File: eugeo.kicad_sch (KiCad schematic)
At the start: 128 parts, among them J1 USB-C, J2 AVR_ISP, SW1 RESET, SW2 BOOT, U1 ATMEGA328P-PU, Y1 16MHz

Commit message: Add centre component cover
Lumberjack-style 2 mm acrylic cover over the diode stacks, MCU and USB-C,
held by four M2 10 mm standoffs. Adds mounting holes H9-H12 to the PCB
(rerouted, DRC clean, 49/49 functional checks), cover outline/DXF/gerbers,
a STEP/STL model, and a clearance check against parts and the case.

Co-Authored-By: Claude Opus 5.5 <noreply@anthropic.com>
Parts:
- added H10, H11, H12, H9: M2, eugeo:MountingHole_M2_NPTH, symbol eugeo:MountingHole
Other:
- note added: "Mounting holes (M2): H1-H8 case / plate, H9-H12 centre cover"
- note removed: "Mounting holes (M2)"
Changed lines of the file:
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@@
     )
   )
-  (text "Mounting holes (M2)" (at 332.74 104.14 0)
+  (text "Mounting holes (M2): H1-H8 case / plate, H9-H12 centre cover" (at 332.74 104.14 0)
     (effects (font (size 2 2)) (justify left bottom))
   )
@@
         )
       )
+    )
+  )
+  (symbol (lib_id "eugeo:MountingHole") (at 337.82 142.24 0) (unit 1)
+    (in_bom no) (on_board yes) (dnp no)
+    (property "Reference" "H9" (at 340.36 140.97 0)
+      (effects (font (size 1.27 1.27)))
+    )
+    (property "Value" "M2" (at 340.36 143.51 0)
+      (effects (font (size 1.27 1.27)))
+    )
+    (property "Footprint" "eugeo:MountingHole_M2_NPTH" (at 337.82 142.24 0)
+      (effects (font (size 1.27 1.27)) hide)
+    )
+    (property "Datasheet" "~" (at 337.82 142.24 0)
+      (effects (font (size 1.27 1.27)) hide)
+    )
+    (instances
+      (project "eugeo"
+        (path "/ac6326a6-577b-5382-9aa2-0aaf148fe34f"
+          (reference "H9") (unit 1)
+        )
+      )
+    )
+  )
+  (symbol (lib_id "eugeo:MountingHole") (at 353.06 142.24 0) (unit 1)
+    (in_bom no) (on_board yes) (dnp no)
+    (property "Reference" "H10" (at 355.6 140.97 0)
+      (effects (font (size 1.27 1.27)))
+    )
+    (property "Value" "M2" (at 355.6 143.51 0)
+      (effects (font (size 1.27 1.27)))
+    )
+    (property "Footprint" "eugeo:MountingHole_M2_NPTH" (at 353.06 142.24 0)
+      (effects (font (size 1.27 1.27)) hide)
+    )
+    (property "Datasheet" "~" (at 353.06 142.24 0)
+      (effects (font (size 1.27 1.27)) hide)
+    )
+    (instances
+      (project "eugeo"
+        (path "/ac6326a6-577b-5382-9aa2-0aaf148fe34f"
+          (reference "H10") (unit 1)
+        )
+      )
+    )
+  )
+  (symbol (lib_id "eugeo:MountingHole") (at 368.3 142.24 0) (unit 1)
+    (in_bom no) (on_board yes) (dnp no)
+    (property "Reference" "H11" (at 370.84 140.97 0)
+      (effects (font (size 1.27 1.27)))
+    )
+    (property "Value" "M2" (at 370.84 143.51 0)
+      (effects (font (size 1.27 1.27)))
+    )
+    (property "Footprint" "eugeo:MountingHole_M2_NPTH" (at 368.3 142.24 0)
+      (effects (font (size 1.27 1.27)) hide)
+    )
+    (property "Datasheet" "~" (at 368.3 142.24 0)
+      (effects (font (size 1.27 1.27)) hide)
+    )
+    (instances
+      (project "eugeo"
+        (path "/ac6326a6-577b-5382-9aa2-0aaf148fe34f"
+          (reference "H11") (unit 1)
+        )
+      )
+    )
+  )
+  (symbol (lib_id "eugeo:MountingHole") (at 383.54 142.24 0) (unit 1)
+    (in_bom no) (on_board yes) (dnp no)
+    (property "Reference" "H12" (at 386.08 140.97 0)
+      (effects (font (size 1.27 1.27)))
+    )
+    (property "Value" "M2" (at 386.08 143.51 0)
+      (effects (font (size 1.27 1.27)))
+    )
+    (property "Footprint" "eugeo:MountingHole_M2_NPTH" (at 383.54 142.24 0)
+      (effects (font (size 1.27 1.27)) hide)
+    )
+    (property "Datasheet" "~" (at 383.54 142.24 0)
+      (effects (font (size 1.27 1.27)) hide)
+    )
+    (instances
+      (project "eugeo"
+        (path "/ac6326a6-577b-5382-9aa2-0aaf148fe34f"
+          (reference "H12") (unit 1)
+        )
+      )

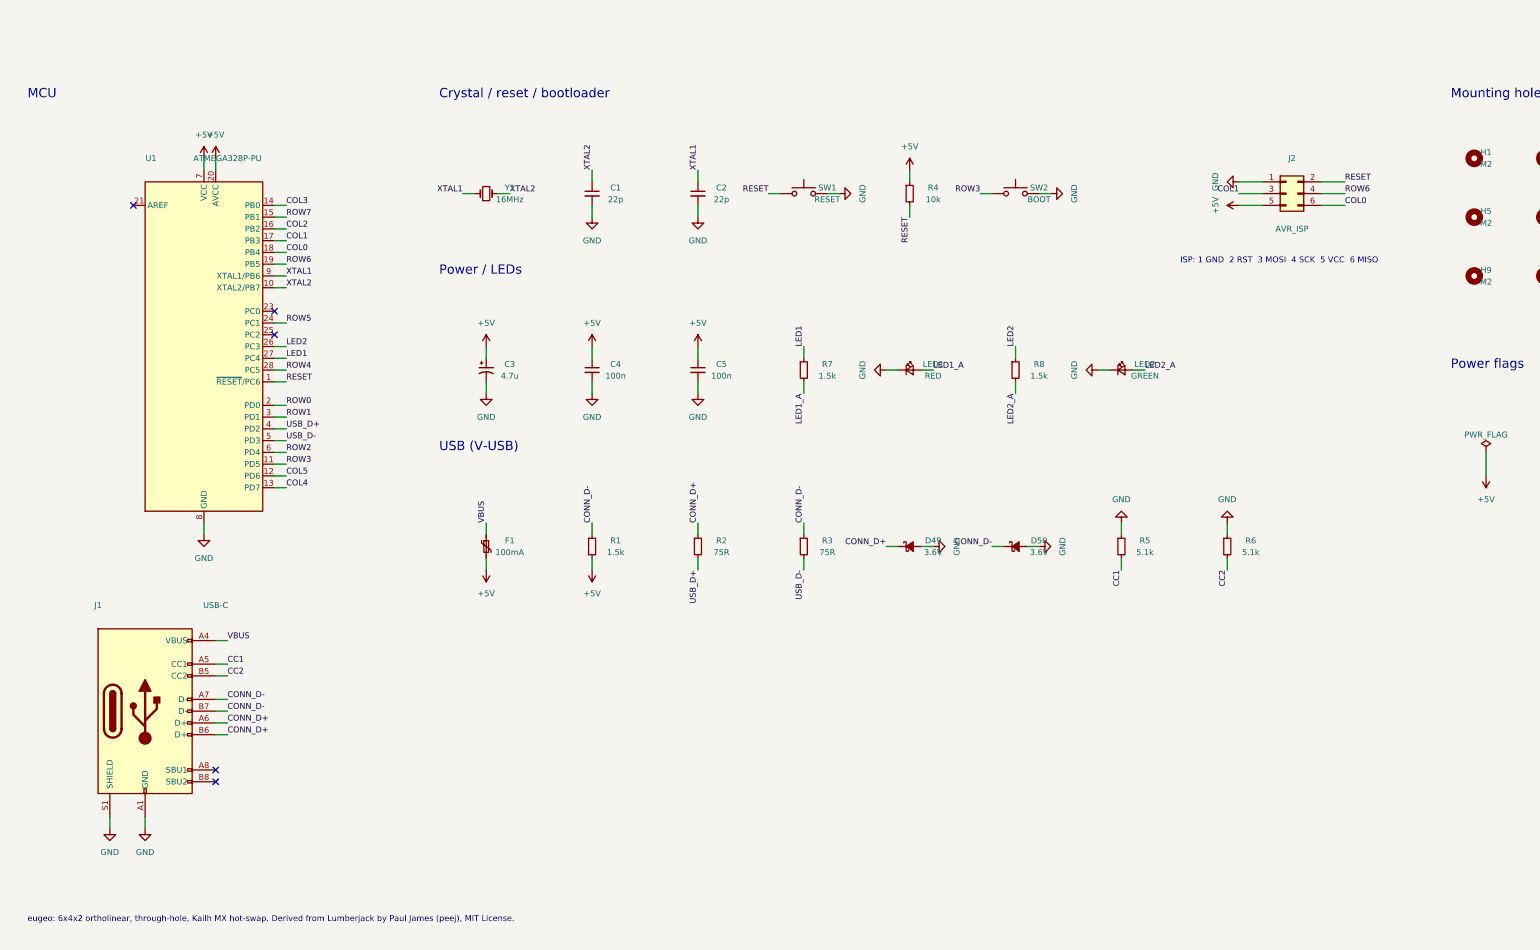
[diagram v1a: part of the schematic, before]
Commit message: Switch to RP2040, zigzag diodes and a frozen-stump back
- MCU: ATmega328P + V-USB -> RP2040 + W25Q16 QSPI flash, 12 MHz crystal,
  MCP1700 3.3 V LDO, USBLC6 ESD and 27R series resistors. SMD parts are
  assembled by JLCPCB (BOM/CPL now include them); everything else stays
  through-hole and on show.
- RP2040 block is hand-routed: +3V3 ring inside the pin ring, +1V1 via the
  back, QSPI / crystal / decoupling / row and column escapes. ISP and SWD
  headers dropped (UF2 flashing over USB with BOOT + RESET).
- Diode stacks zigzag like Lumberjack.
- Back side artwork: frozen tree stump with frost ferns and snowflakes,
  some as bare-copper mask openings (scripts/stump_art.py).
- QMK: RP2040 / rp2040 bootloader, new GP pin map, prebuilt UF2 files.
- verify_design.py rewritten for RP2040 (59 checks), preorder checks 23/23.
- Case support pillar moved clear of U4; cover, plates and laser-cut SVGs
  regenerated for the new cover holes.

Co-Authored-By: Claude Opus 5.5 <noreply@anthropic.com>
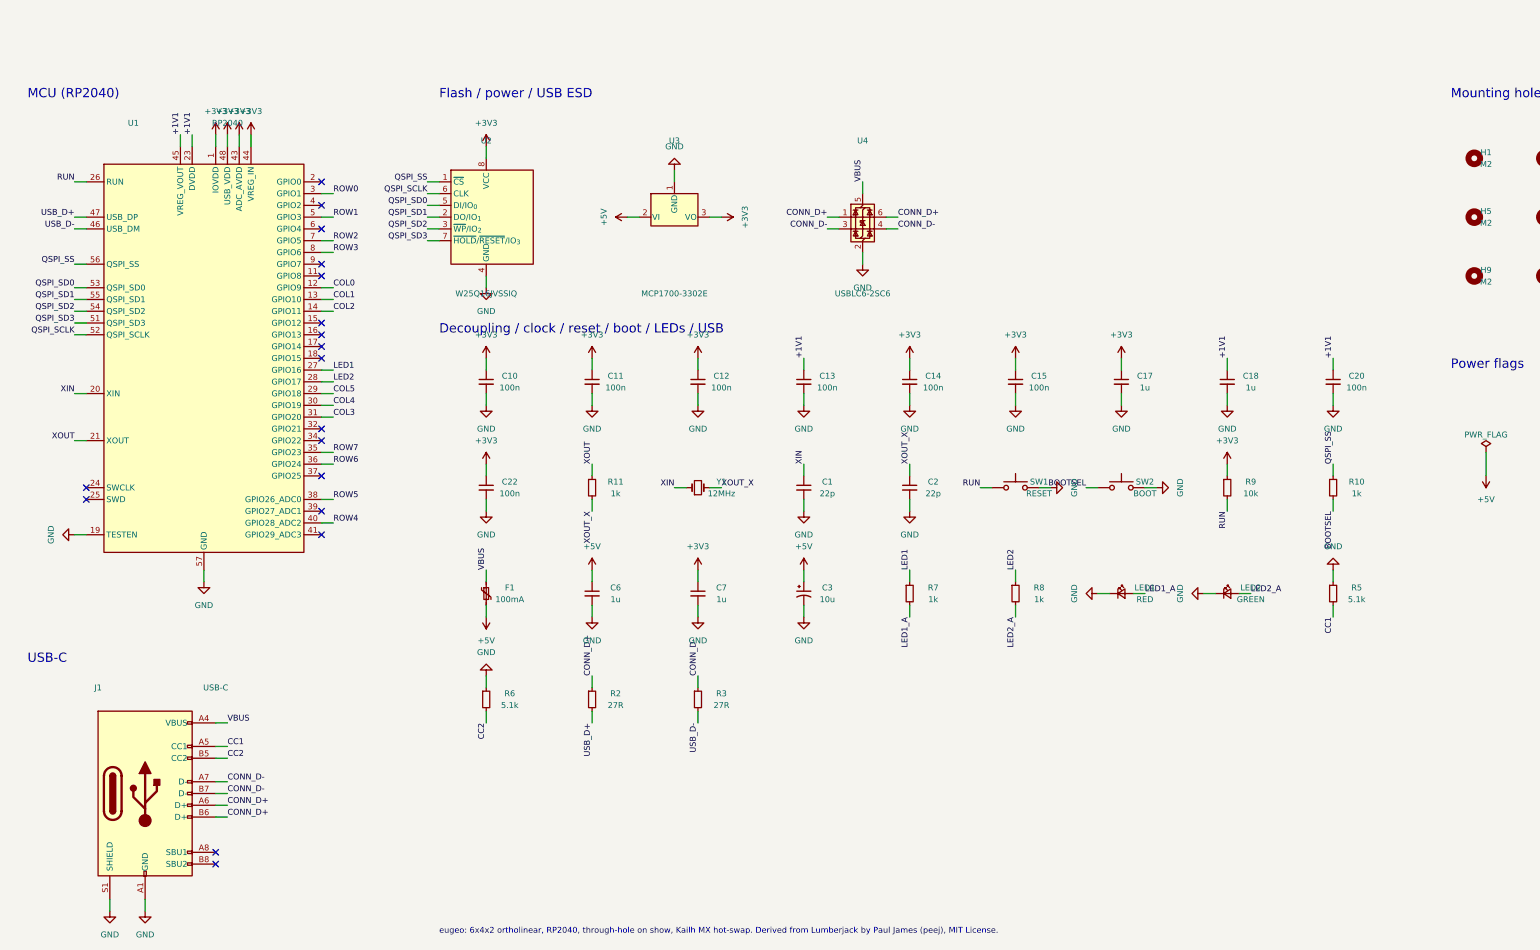
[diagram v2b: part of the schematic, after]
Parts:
- removed C4, C5: 100n, Capacitor_THT:C_Disc_D4.3mm_W1.9mm_P5.00mm, symbol eugeo:C_Small
- removed D49, D50: 3.6V, Diode_THT:D_DO-35_SOD27_P7.62mm_Horizontal, symbol eugeo:D_Zener_Small_ALT
- removed J2: AVR_ISP, Connector_PinHeader_2.54mm:PinHeader_2x03_P2.54mm_Vertical, symbol eugeo:Conn_02x03_Odd_Even
- removed R1: 1.5k, Resistor_THT:R_Axial_DIN0204_L3.6mm_D1.6mm_P7.62mm_Horizontal, symbol eugeo:R_Small
- removed R4: 10k, Resistor_THT:R_Axial_DIN0204_L3.6mm_D1.6mm_P7.62mm_Horizontal, symbol eugeo:R_Small
- added C10, C11, C12, C13, C14, C15, C20, C22: 100n, Capacitor_SMD:C_0402_1005Metric, symbol eugeo:C_Small
- added C17, C18: 1u, Capacitor_SMD:C_0402_1005Metric, symbol eugeo:C_Small
- added C6, C7: 1u, Capacitor_THT:C_Disc_D3.0mm_W2.0mm_P2.50mm, symbol eugeo:C_Small
- added R10: 1k, Resistor_THT:R_Axial_DIN0204_L3.6mm_D1.6mm_P7.62mm_Horizontal, symbol eugeo:R_Small
- added R11: 1k, Resistor_SMD:R_0402_1005Metric, symbol eugeo:R_Small
- added R9: 10k, Resistor_THT:R_Axial_DIN0204_L3.6mm_D1.6mm_P7.62mm_Horizontal, symbol eugeo:R_Small
- added U2: W25Q16JVSSIQ, Package_SO:SOIC-8_5.3x5.3mm_P1.27mm, symbol eugeo:W25Q16JVSS
- added U3: MCP1700-3302E, Package_TO_SOT_THT:TO-92_Inline_Wide, symbol eugeo:MCP1700-3302E_TO
- added U4: USBLC6-2SC6, Package_TO_SOT_SMD:SOT-23-6, symbol eugeo:USBLC6-2SC6
- C3: value 4.7u -> 10u
- R2, R3: value 75R -> 27R
- R7, R8: value 1.5k -> 1k
- U1: value ATMEGA328P-PU -> RP2040; footprint Package_DIP:DIP-28_W7.62mm -> Package_DFN_QFN:QFN-56-1EP_7x7mm_P0.4mm_EP3.2x3.2mm; symbol eugeo:ATmega328P-PU -> eugeo:RP2040
- Y1: value 16MHz -> 12MHz
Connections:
- net +5V: now also C6.1, U3.2 (VI); no longer U1.20 (AVCC), U1.7 (VCC)
- net COL0: now also U1.12 (GPIO9); no longer U1.18 (PB4)
- net COL1: now also U1.13 (GPIO10); no longer U1.17 (PB3)
- net COL2: now also U1.14 (GPIO11); no longer U1.16 (PB2)
- net COL3: now also U1.31 (GPIO20); no longer U1.14 (PB0)
- net COL4: now also U1.30 (GPIO19); no longer U1.13 (PD7)
- net COL5: now also U1.29 (GPIO18); no longer U1.12 (PD6)
- net CONN_D+: now also U4.1 (I/O1), U4.6 (I/O1)
- net CONN_D-: now also U4.3 (I/O2), U4.4 (I/O2)
- net GND: now also U1.19 (TESTEN), U1.57 (GND), C10.2, C11.2, C12.2, C13.2, C14.2, C15.2, C17.2, C18.2, C20.2, C22.2, C6.2, C7.2, U2.4 (GND), U3.1 (GND), U4.2 (GND); no longer U1.22 (GND), U1.8 (GND)
- net LED2: now also U1.28 (GPIO17); no longer U1.26 (PC3)
- net ROW0: now also U1.3 (GPIO1); no longer U1.2 (PD0)
- net ROW1: now also U1.5 (GPIO3); no longer U1.3 (PD1)
- net ROW2: now also U1.7 (GPIO5); no longer U1.6 (PD4)
- net ROW3: now also U1.8 (GPIO6); no longer SW2.1, U1.11 (PD5)
- net ROW4: now also U1.40 (GPIO28_ADC2); no longer U1.28 (PC5)
- net ROW5: now also U1.38 (GPIO26_ADC0); no longer U1.24 (PC1)
- net ROW6: now also U1.36 (GPIO24); no longer U1.19 (PB5)
- net ROW7: now also U1.35 (GPIO23); no longer U1.15 (PB1)
- net USB_D+: now also U1.47 (USB_DP); no longer U1.4 (PD2)
- net USB_D-: now also U1.46 (USB_DM); no longer U1.5 (PD3)
- net VBUS: now also U4.5 (VBUS)
- net XOUT: now reaches U1.21 (XOUT)
- net XOUT: now also R11.1
- net +1V1: now reaches U1.23 (DVDD)
- net +1V1: now also U1.45 (VREG_VOUT), U1.50 (DVDD), C13.1, C18.1, C20.1
- net RESET renamed +3V3
- net +3V3: now also U1.10 (IOVDD), U1.22 (IOVDD), U1.33 (IOVDD), U1.42 (IOVDD), U1.43 (ADC_AVDD), U1.44 (VREG_IN), U1.48 (USB_VDD), U1.49 (IOVDD), C10.1, C11.1, C12.1, C14.1, C15.1, C17.1, C22.1, C7.1, R9.1, U2.8 (VCC), U3.3 (VO); no longer SW1.1
- removed net XTAL1: C2.1, U1.9 (XTAL1/PB6), Y1.1
- removed net XTAL2: C1.1, U1.10 (XTAL2/PB7), Y1.2
- new net BOOTSEL: R10.2, SW2.1
- new net QSPI_SCLK: U1.52 (QSPI_SCLK), U2.6 (CLK)
- new net QSPI_SD0: U1.53 (QSPI_SD0), U2.5 (DI/IO_{0})
- new net QSPI_SD1: U1.55 (QSPI_SD1), U2.2 (DO/IO_{1})
- new net QSPI_SD2: U1.54 (QSPI_SD2), U2.3 (~{WP}/IO_{2})
- new net QSPI_SD3: U1.51 (QSPI_SD3), U2.7 (~{HOLD}/~{RESET}/IO_{3})
- new net QSPI_SS: R10.1, U1.56 (QSPI_SS), U2.1 (~{CS})
- new net RUN: R9.2, SW1.1, U1.26 (RUN)
- new net XIN: C1.1, U1.20 (XIN), Y1.1
- new net XOUT_X: C2.1, R11.2, Y1.2
- no-connect marks 5 -> 18
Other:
- note added: "Decoupling / clock / reset / boot / LEDs / USB"
- note added: "Flash / power / USB ESD"
- note added: "MCU (RP2040)"
- note added: "USB-C"
- note added: "eugeo: 6x4x2 ortholinear, RP2040, through-hole on show, Kailh MX hot-swap. Derived from Lumberjack by Paul James (peej), MIT License."
- note removed: "Crystal / reset / bootloader"
- note removed: "ISP: 1 GND 2 RST 3 MOSI 4 SCK 5 VCC 6 MISO"
- note removed: "MCU"
- note removed: "Power / LEDs"
- note removed: "USB (V-USB)"
- note removed: "eugeo: 6x4x2 ortholinear, through-hole, Kailh MX hot-swap. Derived from Lumberjack by Paul James (peej), MIT License."
- moved on the sheet: C1, C2, C3, F1, J1, LED1, LED2, R2, R3, R5, R6, R7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

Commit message: Move the status LEDs to the top, side by side
LED1 / LED2 now sit next to each other above the QSPI flash. They are
driven from the two topmost left GPIOs (GP2 / GP1) through 0402 resistors
on the back, which frees the crowded bottom-right corner. Left rows move
to GP3-GP6; QMK pins and the UF2 builds follow.

Co-Authored-By: Claude Opus 5.5 <noreply@anthropic.com>
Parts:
- R7, R8: footprint Resistor_THT:R_Axial_DIN0204_L3.6mm_D1.6mm_P7.62mm_Horizontal -> Resistor_SMD:R_0402_1005Metric
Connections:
- net LED1: now also U1.4 (GPIO2); no longer U1.27 (GPIO16)
- net LED2: now also U1.3 (GPIO1); no longer U1.28 (GPIO17)
- net ROW0: now also U1.5 (GPIO3); no longer U1.3 (GPIO1)
- net ROW1: now also U1.6 (GPIO4); no longer U1.5 (GPIO3)
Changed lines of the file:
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@@
     (stroke (width 0) (type default))
   )
-  (label "ROW0" (at 91.44 124.46 0) (fields_autoplaced)
-    (effects (font (size 1.27 1.27)) (justify left bottom))
-  )
-  (no_connect (at 88.9 127))
+  (label "LED2" (at 91.44 124.46 0) (fields_autoplaced)
+    (effects (font (size 1.27 1.27)) (justify left bottom))
+  )
+  (wire (pts (xy 88.9 127) (xy 91.44 127))
+    (stroke (width 0) (type default))
+  )
+  (label "LED1" (at 91.44 127 0) (fields_autoplaced)
+    (effects (font (size 1.27 1.27)) (justify left bottom))
+  )
   (wire (pts (xy 88.9 129.54) (xy 91.44 129.54))
     (stroke (width 0) (type default))
   )
-  (label "ROW1" (at 91.44 129.54 0) (fields_autoplaced)
-    (effects (font (size 1.27 1.27)) (justify left bottom))
-  )
-  (no_connect (at 88.9 132.08))
+  (label "ROW0" (at 91.44 129.54 0) (fields_autoplaced)
+    (effects (font (size 1.27 1.27)) (justify left bottom))
+  )
+  (wire (pts (xy 88.9 132.08) (xy 91.44 132.08))
+    (stroke (width 0) (type default))
+  )
+  (label "ROW1" (at 91.44 132.08 0) (fields_autoplaced)
+    (effects (font (size 1.27 1.27)) (justify left bottom))
+  )
   (wire (pts (xy 88.9 134.62) (xy 91.44 134.62))
     (stroke (width 0) (type default))
@@
   (no_connect (at 88.9 157.48))
   (no_connect (at 88.9 160.02))
-  (wire (pts (xy 88.9 162.56) (xy 91.44 162.56))
-    (stroke (width 0) (type default))
-  )
-  (label "LED1" (at 91.44 162.56 0) (fields_autoplaced)
-    (effects (font (size 1.27 1.27)) (justify left bottom))
-  )
-  (wire (pts (xy 88.9 165.1) (xy 91.44 165.1))
-    (stroke (width 0) (type default))
-  )
-  (label "LED2" (at 91.44 165.1 0) (fields_autoplaced)
-    (effects (font (size 1.27 1.27)) (justify left bottom))
-  )
+  (no_connect (at 88.9 162.56))
+  (no_connect (at 88.9 165.1))
   (wire (pts (xy 88.9 167.64) (xy 91.44 167.64))
     (stroke (width 0) (type default))
@@
       (effects (font (size 1.27 1.27)))
     )
-    (property "Footprint" "Resistor_THT:R_Axial_DIN0204_L3.6mm_D1.6mm_P7.62mm_Horizontal" (at 215.9 210.82 0)
+    (property "Footprint" "Resistor_SMD:R_0402_1005Metric" (at 215.9 210.82 0)
       (effects (font (size 1.27 1.27)) hide)
     )
@@
       (effects (font (size 1.27 1.27)))
     )
-    (property "Footprint" "Resistor_THT:R_Axial_DIN0204_L3.6mm_D1.6mm_P7.62mm_Horizontal" (at 238.76 210.82 0)
-      (effects (font (size 1.27 1.27)) hide)
-    )
+    (property "Footprint" "Resistor_SMD:R_0402_1005Metric" (at 238.76 210.82 0)
+      (effects (font (size 1.27 1.27)) hide)
+    )

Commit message: Balance the centre layout: LEDs left and right, parts mirrored
- One LED on each side at the top (under R5/R6 and R2/R3), driven from the
  topmost left / right GPIO (GP1 / GP28); right rows move to GP23-GP26.
- USB D+/D- go round the right LED to R2/R3.
- Lower parts mirrored about the centre line: U3 | crystal | F1, the four
  disc capacitors in one row, R9 / R10 between RESET and BOOT, C3 centred.

Co-Authored-By: Claude Opus 5.5 <noreply@anthropic.com>
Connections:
- net LED1: now also U1.3 (GPIO1); no longer U1.4 (GPIO2)
- net LED2: now also U1.40 (GPIO28_ADC2); no longer U1.3 (GPIO1)
- net ROW4: now also U1.38 (GPIO26_ADC0); no longer U1.40 (GPIO28_ADC2)
- net ROW5: now also U1.37 (GPIO25); no longer U1.38 (GPIO26_ADC0)
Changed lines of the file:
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@@
     (stroke (width 0) (type default))
   )
-  (label "LED2" (at 91.44 124.46 0) (fields_autoplaced)
+  (label "LED1" (at 91.44 124.46 0) (fields_autoplaced)
     (effects (font (size 1.27 1.27)) (justify left bottom))
   )
-  (wire (pts (xy 88.9 127) (xy 91.44 127))
-    (stroke (width 0) (type default))
-  )
-  (label "LED1" (at 91.44 127 0) (fields_autoplaced)
-    (effects (font (size 1.27 1.27)) (justify left bottom))
-  )
+  (no_connect (at 88.9 127))
   (wire (pts (xy 88.9 129.54) (xy 91.44 129.54))
     (stroke (width 0) (type default))
@@
     (effects (font (size 1.27 1.27)) (justify left bottom))
   )
-  (no_connect (at 88.9 185.42))
+  (wire (pts (xy 88.9 185.42) (xy 91.44 185.42))
+    (stroke (width 0) (type default))
+  )
+  (label "ROW5" (at 91.44 185.42 0) (fields_autoplaced)
+    (effects (font (size 1.27 1.27)) (justify left bottom))
+  )
   (wire (pts (xy 88.9 190.5) (xy 91.44 190.5))
     (stroke (width 0) (type default))
   )
-  (label "ROW5" (at 91.44 190.5 0) (fields_autoplaced)
+  (label "ROW4" (at 91.44 190.5 0) (fields_autoplaced)
     (effects (font (size 1.27 1.27)) (justify left bottom))
   )
@@
     (stroke (width 0) (type default))
   )
-  (label "ROW4" (at 91.44 195.58 0) (fields_autoplaced)
+  (label "LED2" (at 91.44 195.58 0) (fields_autoplaced)
     (effects (font (size 1.27 1.27)) (justify left bottom))
   )
